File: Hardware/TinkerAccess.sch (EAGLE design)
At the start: 45 parts, among them Q1 500mA/300V, Q2 310mA/60V/1.6Ω, U1 SOIC-8SOIC-8

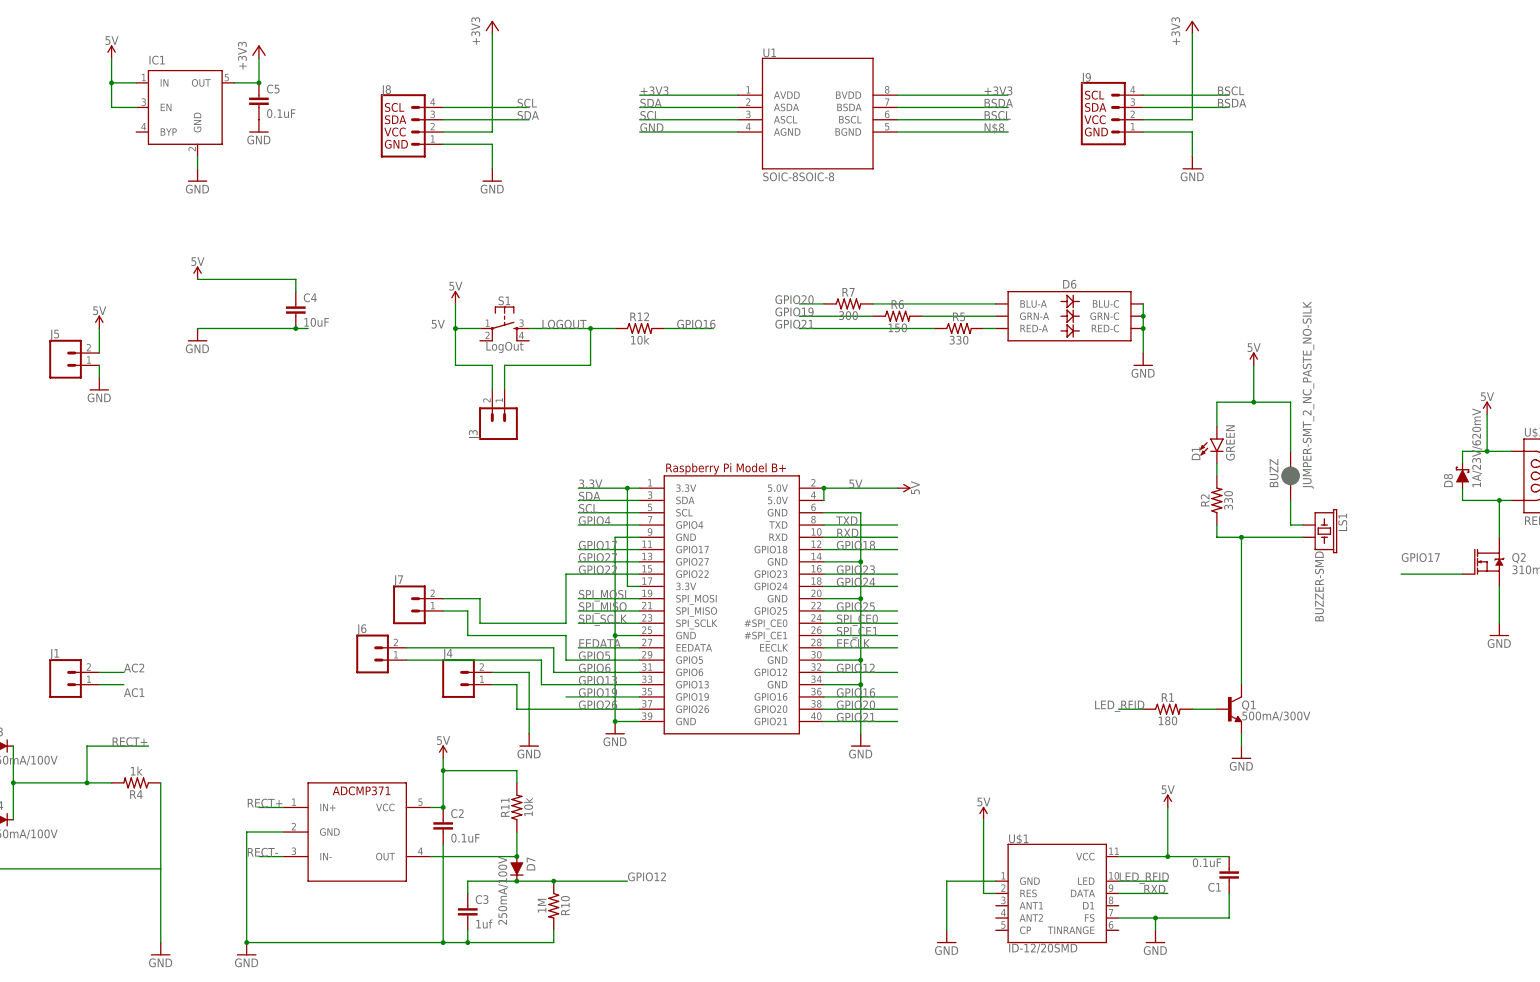
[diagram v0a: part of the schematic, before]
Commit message: Finshied Removing HW bugs
Fixed missing trace, Pad sizes for ADCMP371 and SI8600. Also added a trace for the 3.3V en to a GPIO for restarting the
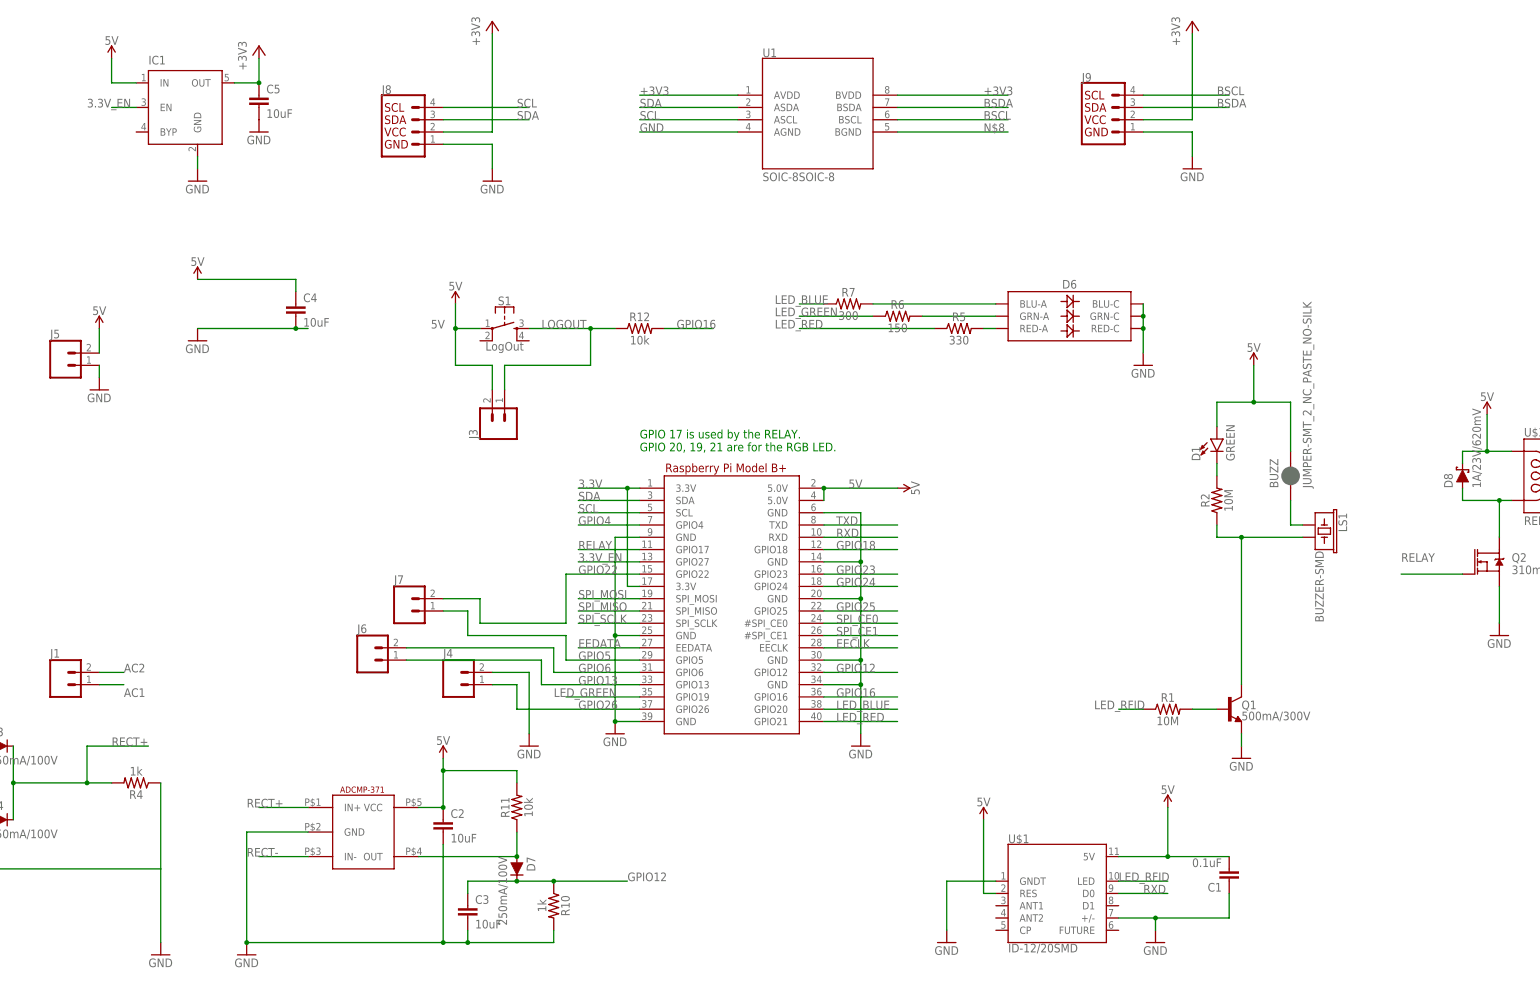
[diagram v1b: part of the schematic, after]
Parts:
- C2, C5: value 0.1uF -> 10uF
- C3: value 1uf -> 10uF
- R1: value 180 -> 10M
- R10: value 1M -> 1k
- R2: value 330 -> 10M
- U$2: value ADCMP371 -> ADCMP-371; device SparkFun-IC-Amplifiers:ADCMP371 -> TinkerMill:ADCMP-371
- U1: device TinkerMill:SI8600 -> TinkerMill:SI8600SO-8
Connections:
- net GPIO17 renamed RELAY
- net GPIO19 renamed LED_GREEN
- net GPIO20 renamed LED_BLUE
- net GPIO21 renamed LED_RED
- removed net GPIO27: RPI1.GPIO27
- new net 3.3V_EN: IC1.EN, RPI1.GPIO27
- net 5V: now also U$1.5V; no longer IC1.EN, U$1.VCC
- net GND: now also U$1.+/-, U$1.GNDT; no longer U$1.FS, U$1.GND
- net RXD: now also U$1.D0; no longer U$1.DATA
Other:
- note added: "GPIO 17 is used by the RELAY. GPIO 20, 19, 21 are for the RGB LED."

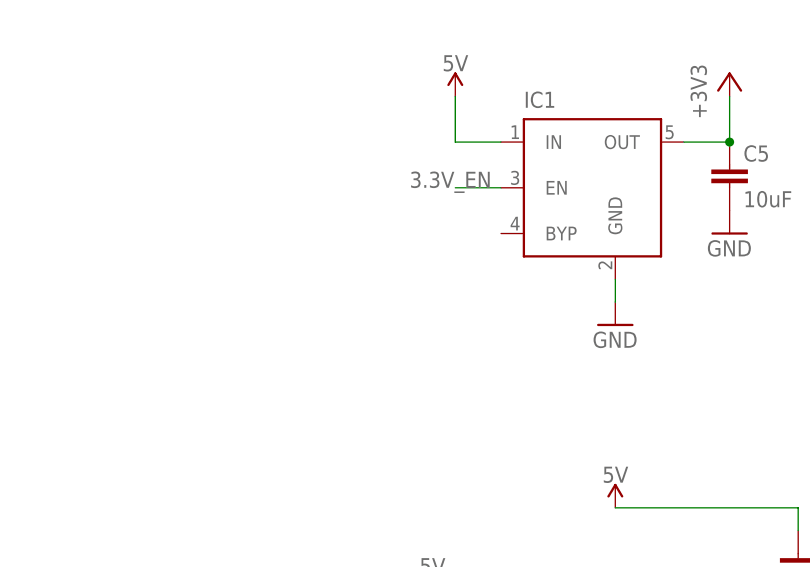
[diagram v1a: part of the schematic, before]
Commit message: added pulldown
Added pulldown resistor to 3v3 Enable line
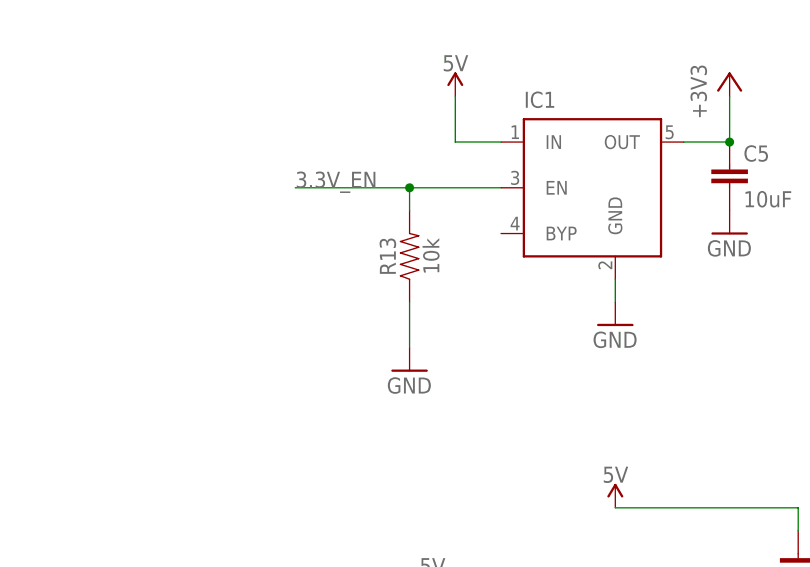
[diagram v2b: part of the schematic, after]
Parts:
- added R13: 10k, SparkFun-Resistors:10KOHM-0603-1/10W-1%
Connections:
- net 3.3V_EN: now also R13.2
- net GND: now also R13.1
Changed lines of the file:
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@@
 <part name="U1" library="TinkerMill" deviceset="SI8600" device="SO-8" package3d_urn="urn:adsk.eagle:package:9206928/1" value="SOIC-8SOIC-8"/>
 <part name="BUZZ" library="SparkFun-Jumpers" library_urn="urn:adsk.eagle:library:528" deviceset="JUMPER-SMT_2_NC_PASTE" device="_NO-SILK" package3d_urn="urn:adsk.eagle:package:39283/1"/>
+<part name="R13" library="SparkFun-Resistors" library_urn="urn:adsk.eagle:library:532" deviceset="10KOHM" device="-0603-1/10W-1%" package3d_urn="urn:adsk.eagle:package:39650/1" value="10k"/>
+<part name="GND17" library="supply1" library_urn="urn:adsk.eagle:library:371" deviceset="GND" device=""/>
 </parts>
 <sheets>
@@
 <attribute name="NAME" x="116.84" y="134.62" size="1.778" layer="95" font="vector" rot="R90"/>
 <attribute name="VALUE" x="121.92" y="134.62" size="1.778" layer="96" font="vector" rot="R90" align="top-left"/>
+</instance>
+<instance part="R13" gate="G$1" x="-129.54" y="205.74" smashed="yes" rot="R90">
+<attribute name="NAME" x="-131.064" y="205.74" size="1.778" layer="95" font="vector" rot="R90" align="bottom-center"/>
+<attribute name="VALUE" x="-128.016" y="205.74" size="1.778" layer="96" font="vector" rot="R90" align="top-center"/>
+</instance>
+<instance part="GND17" gate="1" x="-129.54" y="193.04" smashed="yes">
+<attribute name="VALUE" x="-132.08" y="190.5" size="1.778" layer="96"/>
 </instance>
 </instances>
@@
 <pinref part="U1" gate="G$1" pin="AGND"/>
 </segment>
+<segment>
+<pinref part="R13" gate="G$1" pin="1"/>
+<pinref part="GND17" gate="1" pin="GND"/>
+<wire x1="-129.54" y1="200.66" x2="-129.54" y2="195.58" width="0.1524" layer="91"/>
+</segment>
 </net>
 <net name="TXD" class="0">
@@
 <segment>
 <pinref part="IC1" gate="G1" pin="EN"/>
-<wire x1="-124.46" y1="213.36" x2="-119.38" y2="213.36" width="0.1524" layer="91"/>
-<label x="-129.54" y="213.36" size="1.778" layer="95"/>
-</segment>
-<segment>
+<wire x1="-142.24" y1="213.36" x2="-129.54" y2="213.36" width="0.1524" layer="91"/>
+<label x="-142.24" y="213.36" size="1.778" layer="95"/>
+<pinref part="R13" gate="G$1" pin="2"/>
+<wire x1="-129.54" y1="213.36" x2="-119.38" y2="213.36" width="0.1524" layer="91"/>
+<wire x1="-129.54" y1="210.82" x2="-129.54" y2="213.36" width="0.1524" layer="91"/>
+<junction x="-129.54" y="213.36"/>
+</segment>
+<segment>

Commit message: Changes for v1.4 of TinkerAccess PCB
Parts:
- removed BUZZ: JUMPER-SMT_2_NC_PASTE_NO-SILK, SparkFun-Jumpers:JUMPER-SMT_2_NC_PASTE_NO-SILK
- removed IC1: (no value), v-reg-micrel:MIC5219XX
- removed U$1: ID-12/20SMD, SparkFun-RF:ID-12/20SMD
- removed U$2: ADCMP-371, TinkerMill:ADCMP-371
- removed U$3: RELAY-SPDT-2-G5V, SparkFun-Retired:RELAY-SPDT-2-G5V
- added C10: 0.1uF, SparkFun-Capacitors:0.1UF-0603-25V-(+80/-20%)
- added C6, C8, C9: 1uF, SparkFun-Capacitors:10UF-0603-6.3V-20%
- added C7: 0.1uF, SparkFun-Capacitors:10UF-0603-6.3V-20%
- added D9: 1A/100V, SparkFun-DiscreteSemi:DIODE-BAS16J
- added JP1: BUZZ, SparkFun-Jumpers:JUMPER-SMT_2_NC_PASTE_NO-SILK
- added K1: RELAY-SPDT-2-G5V, SparkFun-Retired:RELAY-SPDT-2-G5V
- added LOGO1: MADE_BY_TINKERMILL, TinkerMill:MADE_BY_TINKERMILL
- added R14: 180, SparkFun-Resistors:10MOHM-0603-1/10W-5%
- added U2: AP2112, v-reg-micrel:MIC5219XX
- added U3: ADCMP-371, TinkerMill:ADCMP-371
- added U4: ID-12/20SMD, SparkFun-RF:ID-12/20SMD
- C1: value 0.1uF -> 10uF; device SparkFun-Capacitors:0.1UF-0603-25V-(+80/-20%) -> SparkFun-Capacitors:10UF-1206-6.3V-20%
- C2, C3: value 10uF -> 0.1uF; device SparkFun-Capacitors:10UF-0603-6.3V-20% -> SparkFun-Capacitors:0.1UF-0603-25V-(+80/-20%)
- C4: value 10uF -> 1uF; device SparkFun-Capacitors:10UF-1206-6.3V-20% -> SparkFun-Capacitors:10UF-0603-6.3V-20%
- C5: value 10uF -> 1uF
- D2, D3, D4, D5, D7: value 250mA/100V -> 1A/100V
- D8: value 1A/23V/620mV -> 1A/100V
- LS1: value BUZZER-SMD -> BUZZER
- R1, R2: value 10M -> 10k; device SparkFun-Resistors:10MOHM-0603-1/10W-5% -> SparkFun-Resistors:10KOHM-0603-1/10W-1%
- R11, R13: device SparkFun-Resistors:10KOHM-0603-1/10W-1% -> SparkFun-Resistors:1KOHM-0603-1/10W-1%
- R12: value 10k -> 1k; device SparkFun-Resistors:10KOHM-0603-1/10W-1% -> SparkFun-Resistors:1KOHM-0603-1/10W-1%
- R3, R4: value 1k -> 10k; device SparkFun-Resistors:1KOHM-0603-1/10W-1% -> SparkFun-Resistors:10KOHM-0603-1/10W-1%
- R5: value 330 -> 300; device SparkFun-Resistors:330OHM-0603-1/10W-1% -> SparkFun-Resistors:300OHM-0603-1/10W-1%
- R7: value 300 -> 330; device SparkFun-Resistors:300OHM-0603-1/10W-1% -> SparkFun-Resistors:330OHM-0603-1/10W-1%
- R8: value 1k -> 330; device SparkFun-Resistors:1KOHM-0603-1/10W-1% -> SparkFun-Resistors:10MOHM-0603-1/10W-5%
- R9: value 1k -> 100k
- U1: value SOIC-8SOIC-8 -> Si8600AC
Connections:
- removed net N$8: U1.BGND
- removed net RECT-: D2.A, D5.A, R8.1, R9.2, U$2.IN-
- new net DETECT: C9.1, D7.C, R10.1, R9.1
- new net VREF: C8.1, R11.2, U3.IN-
- net +3V3: now also C3.2, R1.1, R2.1, U2.OUT; no longer IC1.OUT, J8.VCC, U1.AVDD
- net 3.3V: now also C10.2, C2.2, C6.1, D9.C, J3.2, J8.VCC, R3.1, S1.1, U1.AVDD, U4.5V, U4.RES
- net 3.3V_EN: now also R3.2, U2.EN; no longer IC1.EN, R13.2
- net 5V: now also C1.1, C7.1, JP1.2, K1.2, U2.IN, U3.VCC; no longer BUZZ.2, C1.2, C2.1, IC1.IN, J3.2, R11.2, R8.2, S1.1, U$1.5V, U$1.RES, U$2.VCC, U$3.2
- net AC1: no longer R3.1
- net AC2: no longer R3.2
- net BSCL: now also R2.2
- net BSDA: now also R1.2
- net COMPOUT: now also U3.OUT; no longer R11.1, U$2.OUT
- net GND: now also C1.2, C10.1, C2.1, C3.1, C6.2, C7.2, C8.2, C9.2, D2.A, D5.A, R12.1, R13.2, R9.2, U1.BGND, U2.GND, U3.GND, U4.+/-, U4.GNDT; no longer C1.1, C2.2, C3.2, IC1.GND, R10.2, R13.1, R4.1, R9.1, U$1.+/-, U$1.GNDT, U$2.GND
- net GPIO12: now also D9.A, R10.2; no longer C3.1, D7.C, R10.1
- net GPIO16: now also R4.2; no longer R12.2
- net GPIO18: now also R11.1
- net LED_BLUE: now also R5.1; no longer R7.1
- net LED_RED: now also R7.1; no longer R5.1
- net LED_RFID: now also R14.1, U4.LED; no longer R1.1, U$1.LED
- net LOGOUT: now also R4.1; no longer R12.1
- net N$1: now also R14.2; no longer R1.2
- net N$11: now also R5.2; no longer R7.2
- net N$2: now also JP1.1; no longer BUZZ.1
- net N$3: now also R8.1; no longer R2.1
- net N$4: now also R8.2; no longer R2.2
- net N$5: now also K1.9; no longer U$3.9
- net N$6: now also K1.6; no longer U$3.6
- net N$7: now also K1.10; no longer U$3.10
- net N$9: now also R7.2; no longer R5.2
- net RECT+: now also R12.2, U3.IN+; no longer R4.2, U$2.IN+
- net RELAY: now also R13.1
- net RXD: now also U4.D0; no longer U$1.D0
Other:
- note added: "1.4"
- note added: "GPIO 18 is used by the CURRENT SENSE PWM GPIO 17 is used by the RELAY. GPIO 20, 19, 21 are for the RGB LED."
- note added: "TinkerMill Longmont, CO"
- note removed: "GPIO 17 is used by the RELAY. GPIO 20, 19, 21 are for the RGB LED."
- moved on the sheet: C1, C2, C3, C4, C5, D1, D2, D3, D4, D5, D6, D7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
